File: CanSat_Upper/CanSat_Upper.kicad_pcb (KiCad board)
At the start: 2 copper layers, 50 x 50 mm, 40 parts, among them J1 SERVO1, J10 Power GND, J2 SERVO1, J3 SERVO1, J4 SERVO1, J5 SERVO1, J6 SERVO1, J7 Power 5V, J8 JST_SH_10pin, J9 JST_SH_8pin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

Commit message: v0.2 done
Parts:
- added C14: ?, Capacitor_SMD:C_0603_1608Metric, F.Cu at (120.0, 64.4)
- added C15: ?, Capacitor_SMD:C_0603_1608Metric, F.Cu at (105.8, 64.2)
- added C16: ?, Capacitor_SMD:C_0603_1608Metric, F.Cu at (105.6, 79.0)
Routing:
- net GND: vias 241 -> 243

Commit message: production files done
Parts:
- C14, C15, C16: value ? -> 1u

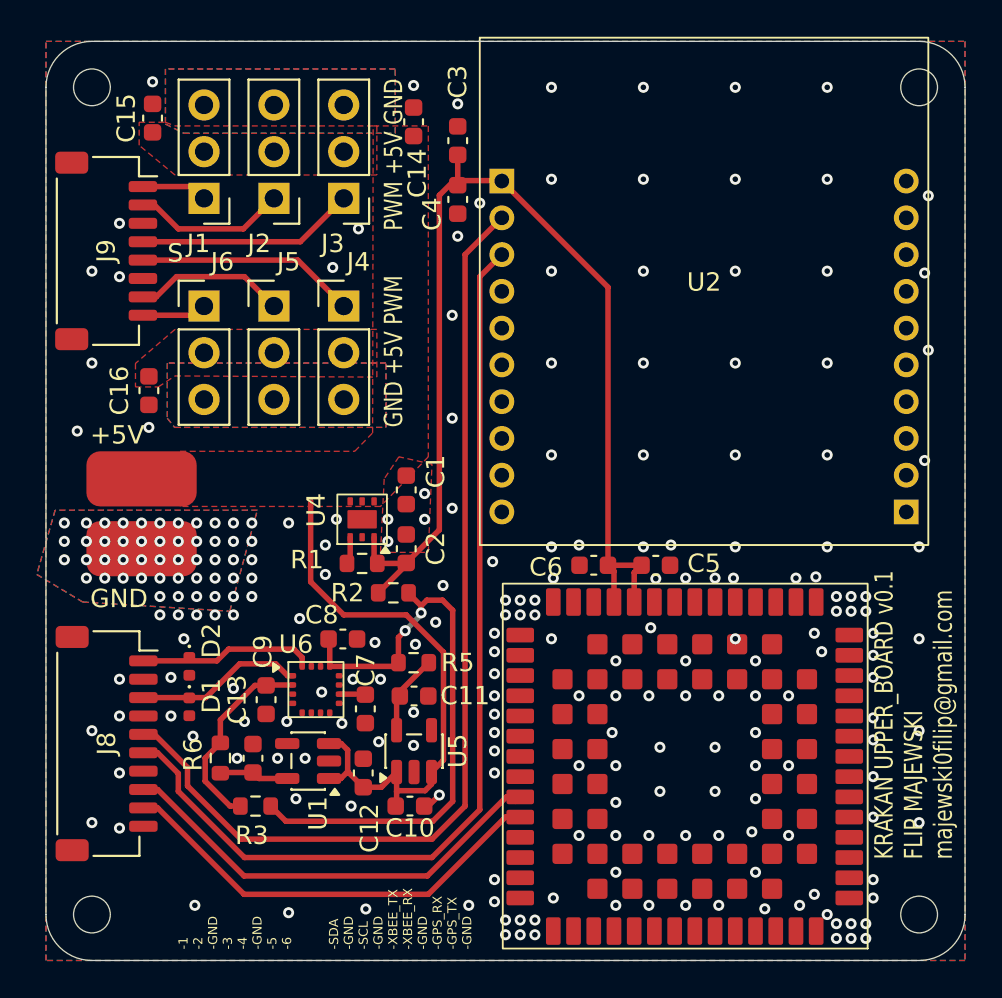
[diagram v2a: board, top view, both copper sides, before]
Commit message: small fixes, added 0resistors to turn on/off radio modeules power
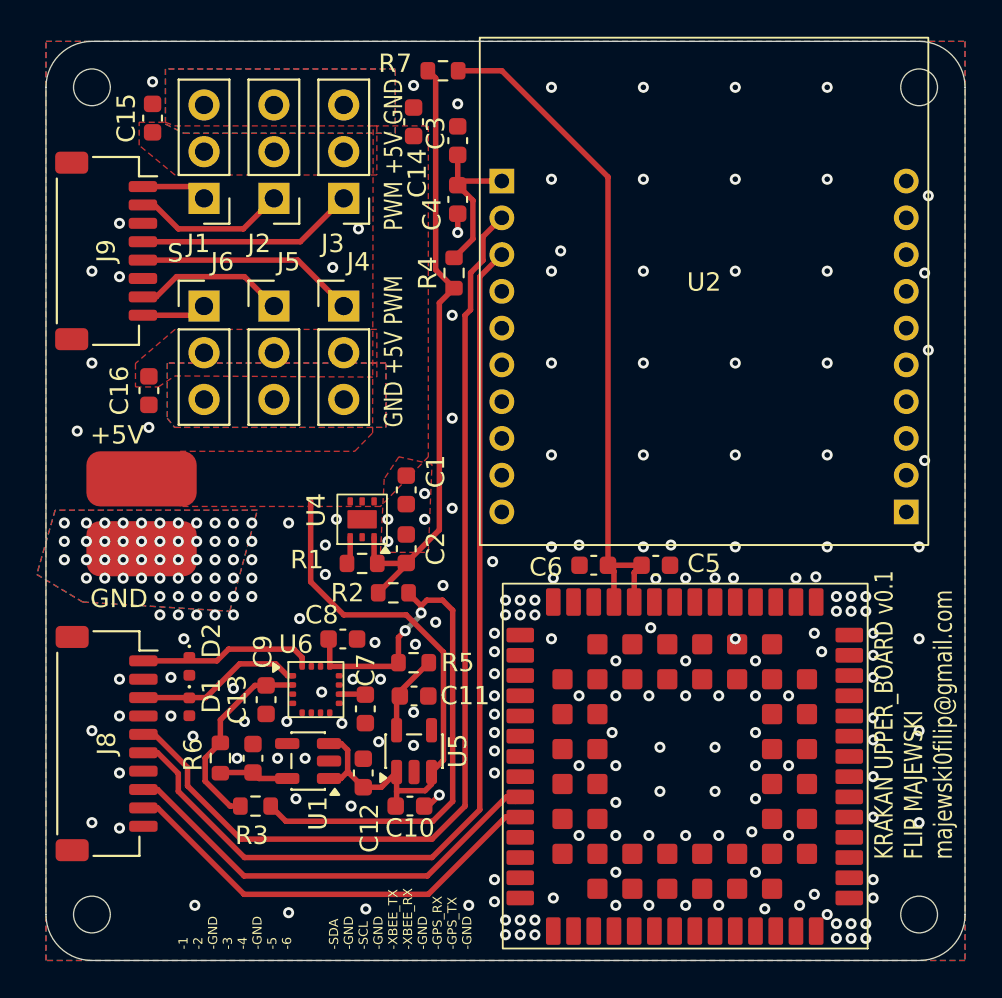
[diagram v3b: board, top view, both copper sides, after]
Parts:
- added R4: 0, Resistor_SMD:R_0603_1608Metric, F.Cu at (122.2, 72.6)
- added R7: 0, Resistor_SMD:R_0603_1608Metric, F.Cu at (121.6, 61.6)
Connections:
- C3 pad 1: +3.3V -> Net-(U2-VCC)
- C4 pad 1: +3.3V -> Net-(U2-VCC)
- C5 pad 1: +3.3V -> Net-(C5-Pad1)
- C6 pad 1: +3.3V -> Net-(C5-Pad1)
- U2 pad 1: +3.3V -> Net-(U2-VCC)
- U3 pad 52: +3.3V -> Net-(C5-Pad1)
- U3 pad 53: +3.3V -> Net-(C5-Pad1)
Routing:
- net Net-(C5-Pad1): track 0.00 -> 37.8 mm
- net +3.3V: track 61.1 -> 34.0 mm
- net Net-(U2-VCC): track 0.00 -> 8.90 mm
- net GND: track 1.07 -> 2.10 mm

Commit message: version 1.1 done
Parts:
- removed C12, C13: 1u, Capacitor_SMD:C_0603_1608Metric
- removed U6: TPS77033PDBV, Package_TO_SOT_SMD:SOT-23-5
- added D3: 5V_YELLOW, Diode_SMD:D_0805_2012Metric, F.Cu at (101.8, 79.2)
- added D4: 3V3_1_BLUE, Diode_SMD:D_0805_2012Metric, F.Cu at (121.2, 91.2)
- added D5: 3V3_2_BLUE, Diode_SMD:D_0805_2012Metric, F.Cu at (121.4, 96.0)
- added D6: GPS_GREEN, Diode_SMD:D_0805_2012Metric, F.Cu at (119.2, 108.4)
- R2, R3, R5, R6: value 0 -> RD; footprint Resistor_SMD:R_0603_1608Metric -> Capacitor_SMD:C_0603_1608Metric
- moved R2 18.7 mm to (103.8, 79.0), turned to 90 degrees
- moved R3 17.2 mm to (121.4, 87.6), turned to -90 degrees
- moved R6 16.3 mm to (122.8, 108.4), turned to 180 degrees
- moved C11 9.33 mm to (112.0, 100.4), turned to 90 degrees
- moved R5 5.97 mm to (121.4, 99.6), turned to 90 degrees
- moved U5 5.33 mm to (115.0, 100.4), turned to 180 degrees
- moved C10 2.07 mm to (118.0, 100.6), turned to 90 degrees
- moved U3 0.20 mm to (143.7, 90.3)
- turned R1 to 180 degrees
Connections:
- C8 pad 1: Net-(U1-DVDD) -> +3.3V2
- C9 pad 1: Net-(U1-AVDD) -> +3.3V2
- R2 pad 1: +3.3V -> +5V
- R2 pad 2: Net-(U1-DVDD) -> Net-(D3-A)
- R3 pad 1: Net-(U1-DVDD) -> +3.3V
- R3 pad 2: Net-(U1-AVDD) -> Net-(D4-A)
- R5 pad 2: Net-(U1-DVDD) -> Net-(D5-A)
- R6 pad 1: +3.3V3 -> /TIMEPULSE
- R6 pad 2: Net-(U1-AVDD) -> Net-(D6-A)
- U1 pad 13: Net-(U1-DVDD) -> +3.3V2
- U1 pad 2: Net-(U1-AVDD) -> +3.3V2
- U3 pad 20: unconnected-(U3-TIMEPULSE-Pad20) -> /TIMEPULSE
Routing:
- net +3.3V2: track 4.40 -> 39.6 mm
- net Net-(U1-DVDD): track 33.3 -> 0.00 mm, vias 2 -> 0
- net /TIMEPULSE: track 0.00 -> 10.9 mm
- net Net-(U1-AVDD): track 10.8 -> 0.00 mm
- net +3.3V3: track 3.73 -> 0.00 mm
- net Net-(D3-A): track 0.00 -> 2.02 mm
- net Net-(D4-A): track 0.00 -> 1.97 mm
- net Net-(D6-A): track 0.00 -> 1.89 mm
- net Net-(D5-A): track 0.00 -> 1.89 mm
- net +5V: track 31.5 -> 32.5 mm
- net /XBEE_TX: track 54.5 -> 53.6 mm
- net GND: track 2.10 -> 2.76 mm, vias 243 -> 240
- net /XBEE_RX: track 53.0 -> 52.4 mm
- net /GPS_RX: track 24.9 -> 24.3 mm
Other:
- board text added: "D_3V3_1"
- board text added: "D_3V3_2"
- board text added: "D_GPS"
